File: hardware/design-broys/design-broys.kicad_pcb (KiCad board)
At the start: 2 copper layers, 1 part, among them U1 ESP32-C3FH4

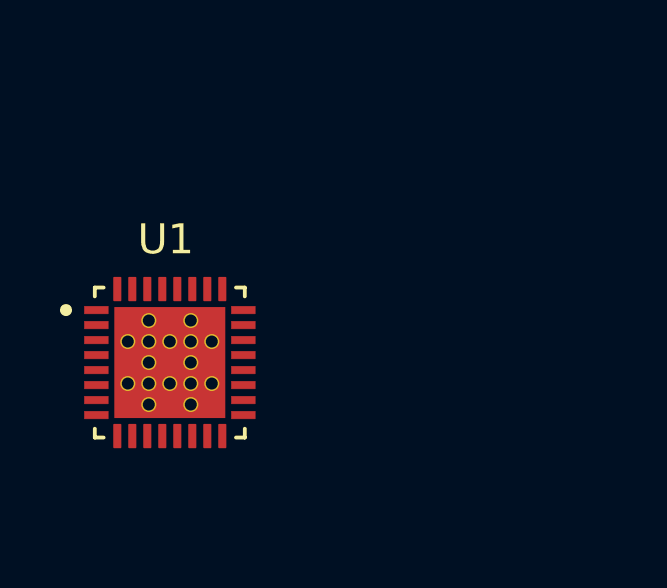
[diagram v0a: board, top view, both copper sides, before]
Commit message: Added external 16MBit flash
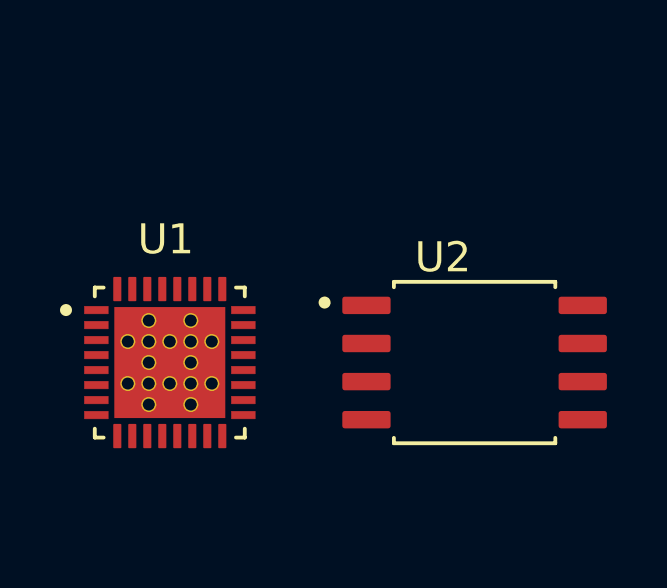
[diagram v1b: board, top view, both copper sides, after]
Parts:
- added U2: W25Q16JVSSIQ, W25Q16JVSSIQ:SOIC127P790X216-8N, F.Cu at (104.1, 78.7)
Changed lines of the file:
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@@
   (net 30 "unconnected-(U1-Pad24)")
   (net 31 "unconnected-(U1-Pad33)")
+  (net 32 "unconnected-(U2-Pad1)")
+  (net 33 "unconnected-(U2-Pad2)")
+  (net 34 "unconnected-(U2-Pad3)")
+  (net 35 "unconnected-(U2-Pad4)")
+  (net 36 "unconnected-(U2-Pad5)")
+  (net 37 "unconnected-(U2-Pad6)")
+  (net 38 "unconnected-(U2-Pad7)")
+  (net 39 "unconnected-(U2-Pad8)")
+  (footprint "W25Q16JVSSIQ:SOIC127P790X216-8N" (layer "F.Cu")
+    (at 104.14 78.74)
+    (property "AVAILABILITY" "Unavailable")
+    (property "DESCRIPTION" "3v 16m-Bit Serial Flash Memory With Dual")
+    (property "MF" "Winbond Electronics")
+    (property "MP" "W25Q16JVSSIQ")
+    (property "PACKAGE" "SOIC-8 Winbond")
+    (property "PRICE" "None")
+    (property "Sheetfile" "design-broys.kicad_sch")
+    (property "Sheetname" "")
+    (attr through_hole)
+    (fp_text reference "U2" (at -1.05616 -3.50582) (layer "F.SilkS")
+      (effects (font (size 1.001087 1.001087) (thickness 0.15)))
+    )
+    (fp_text value "W25Q16JVSSIQ" (at 7.21091 3.507335) (layer "F.Fab")
+      (effects (font (size 1.00152 1.00152) (thickness 0.15)))
+    )
+    (fp_line (start -2.69 -2.69) (end -2.69 -2.51) (layer "F.SilkS") (width 0.127))
+    (fp_line (start 2.69 -2.69) (end 2.69 -2.51) (layer "F.SilkS") (width 0.127))
+    (fp_line (start 2.69 2.51) (end 2.69 2.69) (layer "F.SilkS") (width 0.127))
+    (fp_line (start -2.69 2.69) (end 2.69 2.69) (layer "F.SilkS") (width 0.127))
+    (fp_line (start -2.69 -2.69) (end 2.69 -2.69) (layer "F.SilkS") (width 0.127))
+    (fp_line (start -2.69 2.51) (end -2.69 2.69) (layer "F.SilkS") (width 0.127))
+    (fp_circle (center -5 -2) (end -4.9 -2) (layer "F.SilkS") (width 0.2) (fill none))
+    (fp_line (start -4.66 -2.94) (end 4.66 -2.94) (layer "F.CrtYd") (width 0.05))
+    (fp_line (start -4.66 -2.94) (end -4.66 2.94) (layer "F.CrtYd") (width 0.05))
+    (fp_line (start -4.66 2.94) (end 4.66 2.94) (layer "F.CrtYd") (width 0.05))
+    (fp_line (start 4.66 -2.94) (end 4.66 2.94) (layer "F.CrtYd") (width 0.05))
+    (fp_line (start -2.69 -2.69) (end -2.69 2.69) (layer "F.Fab") (width 0.127))
+    (fp_line (start -2.69 -2.69) (end 2.69 -2.69) (layer "F.Fab") (width 0.127))
+    (fp_line (start -2.69 2.69) (end 2.69 2.69) (layer "F.Fab") (width 0.127))
+    (fp_line (start 2.69 -2.69) (end 2.69 2.69) (layer "F.Fab") (width 0.127))
+    (fp_circle (center -5 -2) (end -4.9 -2) (layer "F.Fab") (width 0.2) (fill none))
+    (pad "1" smd roundrect locked (at -3.605 -1.905) (size 1.61 0.58) (layers "F.Cu" "F.Paste" "F.Mask") (roundrect_rratio 0.14)
+      (net 32 "unconnected-(U2-Pad1)") (pinfunction "~{CS}") (pintype "input"))
+    (pad "2" smd roundrect locked (at -3.605 -0.635) (size 1.61 0.58) (layers "F.Cu" "F.Paste" "F.Mask") (roundrect_rratio 0.14)
+      (net 33 "unconnected-(U2-Pad2)") (pinfunction "DO(IO1)") (pintype "bidirectional"))
+    (pad "3" smd roundrect locked (at -3.605 0.635) (size 1.61 0.58) (layers "F.Cu" "F.Paste" "F.Mask") (roundrect_rratio 0.14)
+      (net 34 "unconnected-(U2-Pad3)") (pinfunction "~{WP}(IO2)") (pintype "bidirectional"))
+    (pad "4" smd roundrect locked (at -3.605 1.905) (size 1.61 0.58) (layers "F.Cu" "F.Paste" "F.Mask") (roundrect_rratio 0.14)
+      (net 35 "unconnected-(U2-Pad4)") (pinfunction "GND") (pintype "power_in"))
+    (pad "5" smd roundrect locked (at 3.605 1.905) (size 1.61 0.58) (layers "F.Cu" "F.Paste" "F.Mask") (roundrect_rratio 0.14)
+      (net 36 "unconnected-(U2-Pad5)") (pinfunction "DI(IO0)") (pintype "bidirectional"))
+    (pad "6" smd roundrect locked (at 3.605 0.635) (size 1.61 0.58) (layers "F.Cu" "F.Paste" "F.Mask") (roundrect_rratio 0.14)
+      (net 37 "unconnected-(U2-Pad6)") (pinfunction "CLK") (pintype "input"))
+    (pad "7" smd roundrect locked (at 3.605 -0.635) (size 1.61 0.58) (layers "F.Cu" "F.Paste" "F.Mask") (roundrect_rratio 0.14)
+      (net 38 "unconnected-(U2-Pad7)") (pinfunction "~{HOLD/RESET}(IO3)") (pintype "bidirectional"))
+    (pad "8" smd roundrect locked (at 3.605 -1.905) (size 1.61 0.58) (layers "F.Cu" "F.Paste" "F.Mask") (roundrect_rratio 0.14)
+      (net 39 "unconnected-(U2-Pad8)") (pinfunction "VCC") (pintype "power_in"))
+    (model "${KICAD6_3DMODEL_DIR}/Package_SO.3dshapes/SO-8_5.3x6.2mm_P1.27mm.step"
+      (offset (xyz 0 0 0))
+      (scale (xyz 1 1 1))
+      (rotate (xyz 0 0 0))
+    )
+  )
   (footprint "ESP32-C3:QFN50P500X500X90-33N" (layer "F.Cu")
     (at 93.98 78.74)
@@
     )
     (fp_poly (pts
+        (xy -1.85 -0.45)
+        (xy -0.95 -0.45)
+        (xy -0.95 0.45)
+        (xy -1.85 0.45)
+      ) (layer "F.Paste") (width 0.01) (fill solid))
+    (fp_poly (pts
+        (xy 0.95 -1.85)
+        (xy 1.85 -1.85)
+        (xy 1.85 -0.95)
+        (xy 0.95 -0.95)
+      ) (layer "F.Paste") (width 0.01) (fill solid))
+    (fp_poly (pts
+        (xy 0.95 0.95)
+        (xy 1.85 0.95)
+        (xy 1.85 1.85)
+        (xy 0.95 1.85)
+      ) (layer "F.Paste") (width 0.01) (fill solid))
+    (fp_poly (pts
+        (xy -0.45 0.95)
+        (xy 0.45 0.95)
+        (xy 0.45 1.85)
+        (xy -0.45 1.85)
+      ) (layer "F.Paste") (width 0.01) (fill solid))
+    (fp_poly (pts
+        (xy -1.85 -1.85)
+        (xy -0.95 -1.85)
+        (xy -0.95 -0.95)
+        (xy -1.85 -0.95)
+      ) (layer "F.Paste") (width 0.01) (fill solid))
+    (fp_poly (pts
+        (xy -0.45 -1.85)
+        (xy 0.45 -1.85)
+        (xy 0.45 -0.95)
+        (xy -0.45 -0.95)
+      ) (layer "F.Paste") (width 0.01) (fill solid))
+    (fp_poly (pts
+        (xy -0.45 -0.45)
+        (xy 0.45 -0.45)
+        (xy 0.45 0.45)
+        (xy -0.45 0.45)
+      ) (layer "F.Paste") (width 0.01) (fill solid))
+    (fp_poly (pts
         (xy 0.95 -0.45)
         (xy 1.85 -0.45)
@@
       ) (layer "F.Paste") (width 0.01) (fill solid))
     (fp_poly (pts
-        (xy 0.95 -1.85)
-        (xy 1.85 -1.85)
-        (xy 1.85 -0.95)
-        (xy 0.95 -0.95)
-      ) (layer "F.Paste") (width 0.01) (fill solid))
-    (fp_poly (pts
-        (xy -1.85 -0.45)
-        (xy -0.95 -0.45)
-        (xy -0.95 0.45)
-        (xy -1.85 0.45)
-      ) (layer "F.Paste") (width 0.01) (fill solid))
-    (fp_poly (pts
-        (xy -0.45 -1.85)
-        (xy 0.45 -1.85)
-        (xy 0.45 -0.95)
-        (xy -0.45 -0.95)
-      ) (layer "F.Paste") (width 0.01) (fill solid))
-    (fp_poly (pts
-        (xy -0.45 0.95)
-        (xy 0.45 0.95)
-        (xy 0.45 1.85)
-        (xy -0.45 1.85)
-      ) (layer "F.Paste") (width 0.01) (fill solid))
-    (fp_poly (pts
-        (xy -0.45 -0.45)
-        (xy 0.45 -0.45)
-        (xy 0.45 0.45)
-        (xy -0.45 0.45)
-      ) (layer "F.Paste") (width 0.01) (fill solid))
-    (fp_poly (pts
         (xy -1.85 0.95)
         (xy -0.95 0.95)
@@
         (xy -1.85 1.85)
       ) (layer "F.Paste") (width 0.01) (fill solid))
-    (fp_poly (pts
-        (xy -1.85 -1.85)
-        (xy -0.95 -1.85)
-        (xy -0.95 -0.95)
-        (xy -1.85 -0.95)
-      ) (layer "F.Paste") (width 0.01) (fill solid))
-    (fp_poly (pts
-        (xy 0.95 0.95)
-        (xy 1.85 0.95)
-        (xy 1.85 1.85)
-        (xy 0.95 1.85)
-      ) (layer "F.Paste") (width 0.01) (fill solid))
-    (fp_line (start 2.5 2.5) (end 2.5 2.205) (layer "F.SilkS") (width 0.127))
-    (fp_line (start 2.5 -2.5) (end 2.205 -2.5) (layer "F.SilkS") (width 0.127))
     (fp_line (start 2.5 2.5) (end 2.205 2.5) (layer "F.SilkS") (width 0.127))
-    (fp_line (start -2.5 2.5) (end -2.205 2.5) (layer "F.SilkS") (width 0.127))
-    (fp_line (start -2.5 -2.5) (end -2.5 -2.205) (layer "F.SilkS") (width 0.127))
     (fp_line (start 2.5 -2.5) (end 2.5 -2.205) (layer "F.SilkS") (width 0.127))
     (fp_line (start -2.5 -2.5) (end -2.205 -2.5) (layer "F.SilkS") (width 0.127))
+    (fp_line (start 2.5 -2.5) (end 2.205 -2.5) (layer "F.SilkS") (width 0.127))
+    (fp_line (start 2.5 2.5) (end 2.5 2.205) (layer "F.SilkS") (width 0.127))
     (fp_line (start -2.5 2.5) (end -2.5 2.205) (layer "F.SilkS") (width 0.127))
+    (fp_line (start -2.5 -2.5) (end -2.5 -2.205) (layer "F.SilkS") (width 0.127))
+    (fp_line (start -2.5 2.5) (end -2.205 2.5) (layer "F.SilkS") (width 0.127))
     (fp_circle (center -3.46 -1.75) (end -3.36 -1.75) (layer "F.SilkS") (width 0.2) (fill none))
+    (fp_line (start -3.105 3.105) (end -3.105 -3.105) (layer "F.CrtYd") (width 0.05))
     (fp_line (start 3.105 3.105) (end 3.105 -3.105) (layer "F.CrtYd") (width 0.05))
-    (fp_line (start -3.105 3.105) (end -3.105 -3.105) (layer "F.CrtYd") (width 0.05))
     (fp_line (start -3.105 -3.105) (end 3.105 -3.105) (layer "F.CrtYd") (width 0.05))
     (fp_line (start -3.105 3.105) (end 3.105 3.105) (layer "F.CrtYd") (width 0.05))
+    (fp_line (start -2.5 2.5) (end -2.5 -2.5) (layer "F.Fab") (width 0.127))
     (fp_line (start 2.5 2.5) (end -2.5 2.5) (layer "F.Fab") (width 0.127))
+    (fp_line (start 2.5 2.5) (end 2.5 -2.5) (layer "F.Fab") (width 0.127))
     (fp_line (start 2.5 -2.5) (end -2.5 -2.5) (layer "F.Fab") (width 0.127))
-    (fp_line (start 2.5 2.5) (end 2.5 -2.5) (layer "F.Fab") (width 0.127))
-    (fp_line (start -2.5 2.5) (end -2.5 -2.5) (layer "F.Fab") (width 0.127))
     (fp_circle (center -3.46 -1.75) (end -3.36 -1.75) (layer "F.Fab") (width 0.2) (fill none))
     (pad "1" smd roundrect locked (at -2.45 -1.75) (size 0.81 0.27) (layers "F.Cu" "F.Paste" "F.Mask") (roundrect_rratio 0.03)
@@
     (pad "48" thru_hole circle locked (at -0.7 1.4) (size 0.5 0.5) (drill 0.4) (layers *.Cu))
     (pad "49" thru_hole circle locked (at 0.7 1.4) (size 0.5 0.5) (drill 0.4) (layers *.Cu))
-    (model "/home/borisnotes/projects/Broys/hardware/kicad-parts/ESP32-C3/ESP32-C3FH4.step"
-      (offset (xyz 0.05 0 0))
-      (scale (xyz 1 1 1))
-      (rotate (xyz -90 0 0))
-    )
   )
 )

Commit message: Fixed the issue with kicad versioning
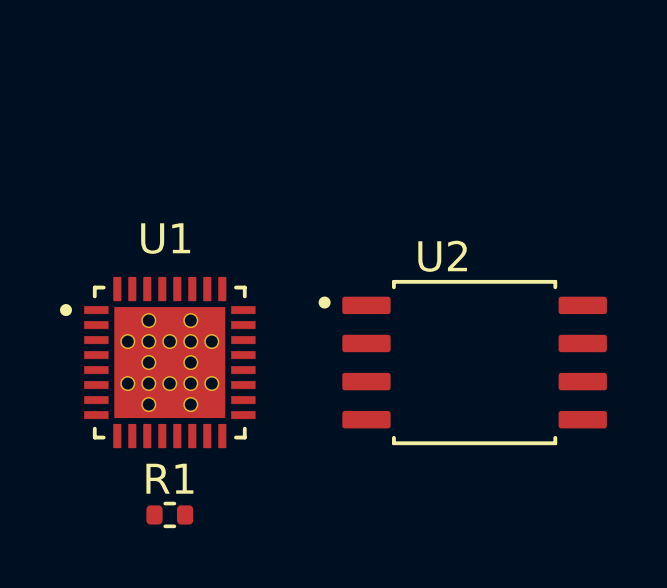
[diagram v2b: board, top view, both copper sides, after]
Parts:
- added R1: 10k, Resistor_SMD:R_0402_1005Metric, F.Cu at (94.0, 83.8)
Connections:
- U1 pad 11: unconnected-(U1-Pad11) -> +3V3
- U1 pad 17: unconnected-(U1-Pad17) -> +3V3
- U1 pad 2: Net-(U1-Pad2) -> +3.3VA
- U1 pad 3: Net-(U1-Pad2) -> +3.3VA
- U1 pad 31: Net-(U1-Pad31) -> +3.3VA
- U1 pad 32: Net-(U1-Pad31) -> +3.3VA
- U1 pad 33: unconnected-(U1-Pad33) -> GND
- U1 pad 7: unconnected-(U1-Pad7) -> Net-(U1-Pad7)
- U2 pad 4: unconnected-(U2-Pad4) -> GND
- U2 pad 8: unconnected-(U2-Pad8) -> +3V3

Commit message: Added LEDs for the first digit.
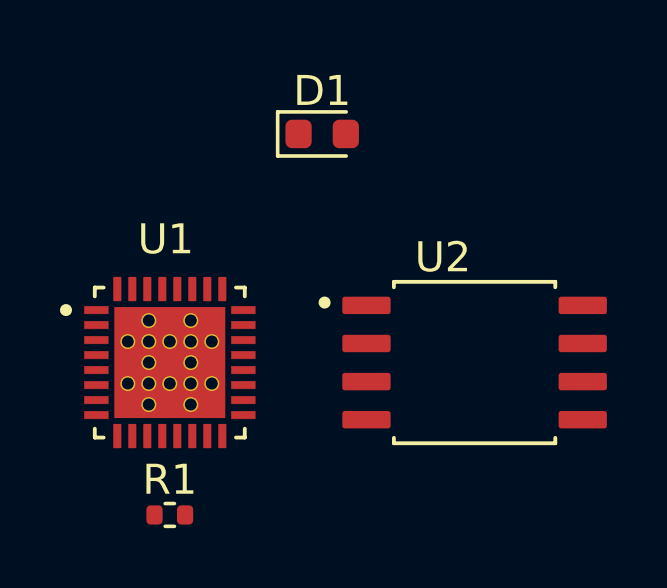
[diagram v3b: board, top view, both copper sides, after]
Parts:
- added D1: LED, LED_SMD:LED_0603_1608Metric, F.Cu at (99.1, 71.1)
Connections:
- U1 pad 21: unconnected-(U1-Pad21) -> CS-memory
- U1 pad 22: unconnected-(U1-Pad22) -> SPICLK-memory
- U1 pad 23: unconnected-(U1-Pad23) -> DI-memory
- U1 pad 24: unconnected-(U1-Pad24) -> DO-memory
- U2 pad 1: unconnected-(U2-Pad1) -> CS-memory
- U2 pad 2: unconnected-(U2-Pad2) -> DO-memory
- U2 pad 5: unconnected-(U2-Pad5) -> DI-memory
- U2 pad 6: unconnected-(U2-Pad6) -> SPICLK-memory
